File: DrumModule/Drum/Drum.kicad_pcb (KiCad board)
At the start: 2 copper layers, 39.4 x 99.1 mm, 44 parts, among them J1 Barrel_Jack_Switch, J2 Barrel_Jack_Switch, J3 Conn_02x05_Odd_Even, J4 Barrel_Jack_Switch, J5 Barrel_Jack_Switch, Q1 MMBT3904, Q2 MMBT3904, U1 74HC74, U2 MIC5205-5.0YM5, U3 LM2904DR, U4 LM2904DR

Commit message: Worked on the Drum
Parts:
- removed J4, J5: Barrel_Jack_Switch, Eurocad:PJ301M-12
- removed Q2: MMBT3904, Package_TO_SOT_SMD:SOT-23
- removed R13: 4.7M, Resistor_SMD:R_0805_2012Metric
- removed R14: 1k, Resistor_SMD:R_0805_2012Metric
- removed R15, R16, R17, R18: 10k, Resistor_SMD:R_0805_2012Metric
- added C14: 1uF, Capacitor_SMD:C_0805_2012Metric, F.Cu at (194.7, 91.9)
- added C15: 1uF, Capacitor_SMD:C_0805_2012Metric, F.Cu at (229.5, 65.7)
- added C16: 1uF, Capacitor_SMD:C_0805_2012Metric, F.Cu at (198.2, 91.9)
- added RV1: 5k, Eurocad:Alpha9mmPot, F.Cu at (210.4, 82.8)
- added RV2: 1M, Eurocad:Alpha9mmPot, F.Cu at (198.8, 69.7)
- added RV3: 50k, Eurocad:Alpha9mmPot, F.Cu at (222.0, 69.7)
- added RV4: 50k, Eurocad:Alpha9mmPot, F.Cu at (184.2, 101.6)
- added RV5: 50k, Eurocad:Alpha9mmPot, F.Cu at (210.4, 69.7)
- added U5: LM2904DR, Package_SO:SOIC-8_3.9x4.9mm_P1.27mm, F.Cu at (120.7, 73.7)
- C7: value 22nF -> 68nF
- C8: value 68nF -> 1uF
- C9: value 22nF -> 1uF
- R11, R3, R4: value 1M -> 10k
- R12: value 2k2 -> 10k
- R2: value 100k -> 1M
- R6: value 10k -> 1M
- R7: value 10k -> 1k
- R9: value 10k -> 5k
- moved J2 48.0 mm to (171.4, 55.9), turned to 180 degrees
- moved U3 39.7 mm to (118.1, 57.1)
- moved U1 31.2 mm to (127.0, 82.5)
- moved J1 0.57 mm to (144.8, 55.9), turned to 180 degrees
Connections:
- C10 pad 1: +12V -> Net-(C10-Pad1)
- C10 pad 2: GND -> Net-(C10-Pad2)
- C11 pad 1: GND -> +12V
- C11 pad 2: -12V -> GND
- C7 pad 2: Net-(C7-Pad2) -> Net-(C6-Pad1)
- C8 pad 1: Net-(C8-Pad1) -> +12V
- C8 pad 2: Net-(C6-Pad1) -> GND
- C9 pad 1: Net-(C9-Pad1) -> GND
- C9 pad 2: Net-(C7-Pad1) -> -12V
- J1 pad 1: Net-(J1-Pad1) -> GND
- J1 pad 2: GND -> Net-(J1-Pad2)
- J2 pad 1: Net-(J2-Pad1) -> GND
- J2 pad 2: GND -> Net-(J2-Pad2)
- J2 pad 3: Net-(J2-Pad3) -> Net-(C10-Pad2)
- Q1 pad 2: GND -> Net-(Q1-Pad2)
- Q1 pad 3: Net-(Q1-Pad3) -> +5V
- R1 pad 2: Net-(J1-Pad1) -> Net-(J1-Pad3)
- R10 pad 2: GND -> Net-(C10-Pad1)
- R11 pad 1: Net-(C6-Pad2) -> Net-(R11-Pad1)
- R11 pad 2: Net-(C8-Pad1) -> Net-(C15-Pad2)
- R12 pad 1: GND -> Net-(R12-Pad1)
- R12 pad 2: Net-(C6-Pad1) -> Net-(C16-Pad1)
- R2 pad 1: Net-(Q2-Pad1) -> Net-(Q1-Pad1)
- R2 pad 2: Net-(J2-Pad1) -> GND
- R3 pad 2: Net-(Q1-Pad1) -> Net-(Q1-Pad2)
- R4 pad 1: GND -> Net-(R4-Pad1)
- R4 pad 2: Net-(Q2-Pad1) -> Net-(R4-Pad2)
- R5 pad 1: Net-(Q1-Pad3) -> Net-(R4-Pad2)
- R5 pad 2: +5V -> GND
- R6 pad 1: Net-(Q2-Pad3) -> Net-(C6-Pad2)
- R6 pad 2: +5V -> Net-(R6-Pad2)
- R7 pad 2: Net-(R7-Pad2) -> Net-(C6-Pad1)
- R8 pad 1: Net-(R8-Pad1) -> Net-(C7-Pad1)
- R8 pad 2: Net-(R10-Pad1) -> Net-(R8-Pad2)
- R9 pad 1: Net-(R7-Pad2) -> Net-(R8-Pad2)
- R9 pad 2: GND -> Net-(R9-Pad2)
- U1 pad 10: +5V -> (no net)
- U1 pad 11: Net-(Q2-Pad3) -> (no net)
- U1 pad 12: Net-(U1-Pad12) -> (no net)
- U1 pad 13: +5V -> (no net)
- U1 pad 3: Net-(Q1-Pad3) -> Net-(Q1-Pad2)
- U1 pad 5: Net-(R7-Pad1) -> Net-(R4-Pad1)
- U1 pad 8: Net-(U1-Pad12) -> (no net)
- U1 pad 9: Net-(R8-Pad1) -> (no net)
- U3 pad 2: Net-(R15-Pad2) -> Net-(R8-Pad2)
- U3 pad 5: Net-(R7-Pad2) -> Net-(R4-Pad2)
- U3 pad 7: Net-(C8-Pad1) -> Net-(C7-Pad1)
- U4 pad 1: Net-(J5-Pad1) -> Net-(R10-Pad1)
- U4 pad 2: GND -> Net-(R10-Pad1)
- U4 pad 3: Net-(R16-Pad2) -> Net-(C15-Pad2)
- U4 pad 5: Net-(R10-Pad1) -> Net-(C16-Pad1)
- U4 pad 6: Net-(C7-Pad2) -> Net-(C15-Pad1)
- U4 pad 7: Net-(C9-Pad1) -> Net-(C15-Pad1)
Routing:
- net -12V: track 133.4 -> 53.0 mm
- net +12V: track 124.2 -> 76.9 mm, vias 7 -> 4
- net Net-(Q2-Pad3): track 39.4 -> 0.00 mm, vias 4 -> 0
- net +5V: track 81.7 -> 44.5 mm
- net Net-(RV3-Pad1): track 29.1 -> 0.00 mm, vias 2 -> 0
- net Net-(J5-Pad1): track 28.3 -> 0.00 mm, vias 2 -> 0
- net Net-(R10-Pad1): track 27.2 -> 54.1 mm, vias 2 -> 4
- net Net-(R7-Pad2): track 27.9 -> 2.12 mm, vias 2 -> 0
- net Net-(C8-Pad1): track 16.3 -> 0.00 mm
- net Net-(C15-Pad2): track 0.00 -> 10.5 mm
- net Net-(C6-Pad2): track 11.0 -> 21.3 mm, vias 0 -> 2
- net Net-(R15-Pad2): track 9.31 -> 0.00 mm, vias 1 -> 0
- net Net-(U1-Pad12): track 9.29 -> 0.00 mm
- net Net-(R16-Pad2): track 8.24 -> 0.00 mm
- net Net-(Q1-Pad3): track 18.1 -> 11.7 mm
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
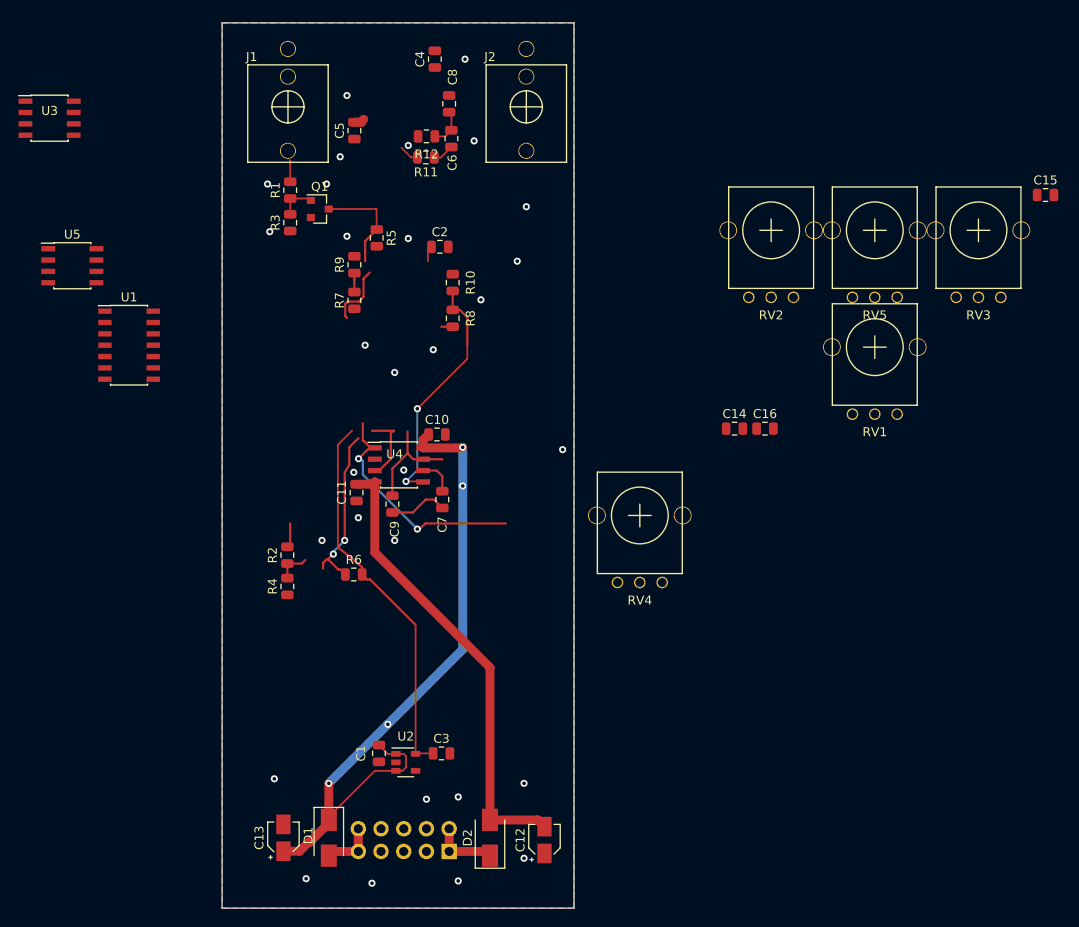
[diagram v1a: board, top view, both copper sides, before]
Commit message: Organized layout of drum, should be ready for routing.
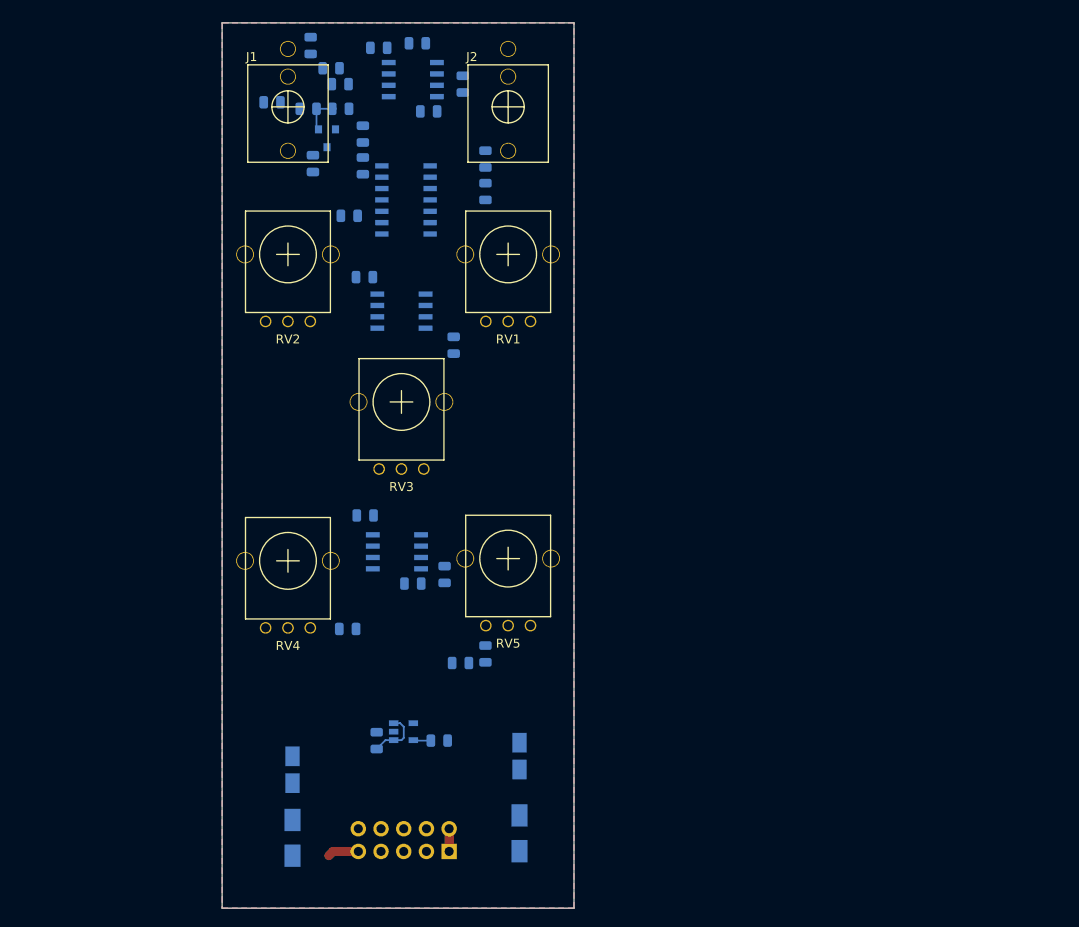
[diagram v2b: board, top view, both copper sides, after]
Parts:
- C1, C10, C11, C12, C13, C14, C15, C16, C2, C3, C4, C5, C6, C7, C8, C9, D1, D2, Q1, R1, R10, R11, R12, R2, R3, R4, R5, R6, R7, R8, R9, U1, U2, U3, U4, U5: moved to B.Cu
- moved C15 79.5 mm to (162.3, 108.2), turned to 270 degrees
- moved RV3 67.4 mm to (157.5, 88.9)
- moved R12 58.3 mm to (166.9, 117.1), turned to 270 degrees
- moved R6 56.7 mm to (149.6, 51.6), turned to 180 degrees
- moved RV5 55.1 mm to (169.4, 106.4)
- moved RV2 54.1 mm to (144.8, 72.4)
- moved C8 53.8 mm to (158.8, 109.2), turned to 180 degrees
- moved R11 53.5 mm to (151.5, 114.3), turned to 0 degrees
- moved C7 52.9 mm to (147.3, 49.0), turned to 270 degrees
- moved R4 47.8 mm to (153.2, 62.5)
- moved C14 44.7 mm to (153.3, 74.9)
- moved R2 43.9 mm to (147.6, 62.2), turned to 270 degrees
- moved C16 43.0 mm to (164.1, 118.1), turned to 180 degrees
- moved RV1 42.3 mm to (169.4, 72.4)
- moved U3 40.9 mm to (158.8, 52.8), turned to 180 degrees
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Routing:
- net +12V: track 76.9 -> 6.09 mm, vias 4 -> 0
- net Net-(R10-Pad1): track 54.1 -> 0.00 mm, vias 4 -> 0
- net -12V: track 53.0 -> 0.00 mm
- net +5V: track 44.5 -> 1.98 mm
- net Net-(C6-Pad2): track 21.3 -> 0.00 mm, vias 2 -> 0
- net Net-(C9-Pad1): track 12.1 -> 0.00 mm
- net Net-(Q1-Pad3): track 11.7 -> 0.00 mm
- net Net-(C15-Pad2): track 10.5 -> 0.00 mm
- net Net-(C7-Pad1): track 7.85 -> 0.00 mm
- net Net-(U1-Pad2): track 7.04 -> 0.00 mm
- net Net-(D2-Pad1): track 7.31 -> 2.54 mm
- net Net-(C6-Pad1): track 4.26 -> 0.00 mm
- net Net-(C7-Pad2): track 4.09 -> 0.00 mm
- net Net-(Q2-Pad1): track 3.79 -> 0.00 mm
- net GND: track 2.75 -> 0.00 mm, vias 30 -> 0
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
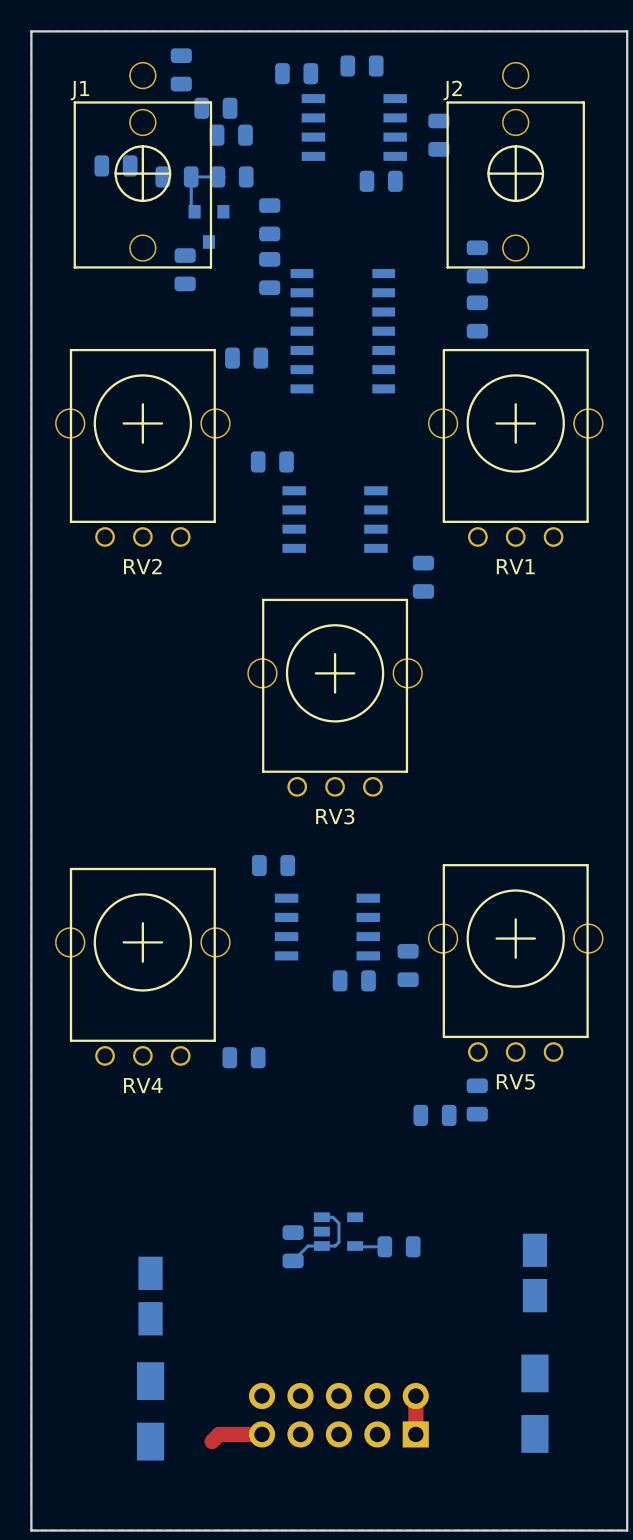
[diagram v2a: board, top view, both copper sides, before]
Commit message: worked on the layout of the drum
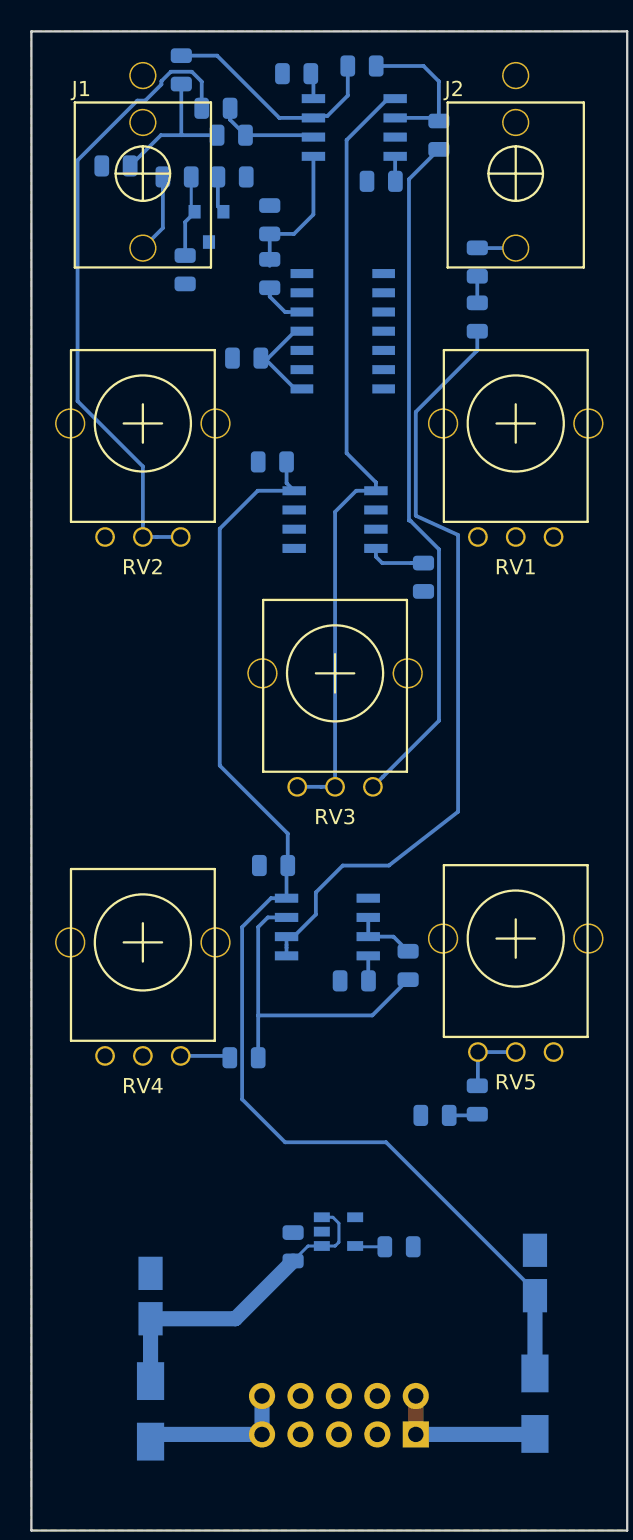
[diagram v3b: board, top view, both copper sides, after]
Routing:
- net -12V: track 0.00 -> 81.2 mm
- net Net-(RV3-Pad1): track 0.00 -> 52.3 mm
- net Net-(R10-Pad1): track 0.00 -> 51.9 mm
- net Net-(R9-Pad2): track 0.00 -> 45.6 mm
- net Net-(R6-Pad2): track 0.00 -> 42.0 mm
- net +12V: track 6.09 -> 28.4 mm
- net Net-(C15-Pad2): track 0.00 -> 21.7 mm
- net Net-(C7-Pad1): track 0.00 -> 15.3 mm
- net Net-(R8-Pad2): track 0.00 -> 10.2 mm
- net Net-(C6-Pad1): track 0.00 -> 9.97 mm
- net Net-(R4-Pad2): track 0.00 -> 9.37 mm
- net Net-(D2-Pad1): track 2.54 -> 10.4 mm
- net +5V: track 1.98 -> 8.99 mm
- net Net-(C6-Pad2): track 0.00 -> 6.85 mm
- net Net-(D1-Pad2): track 3.50 -> 10.1 mm
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
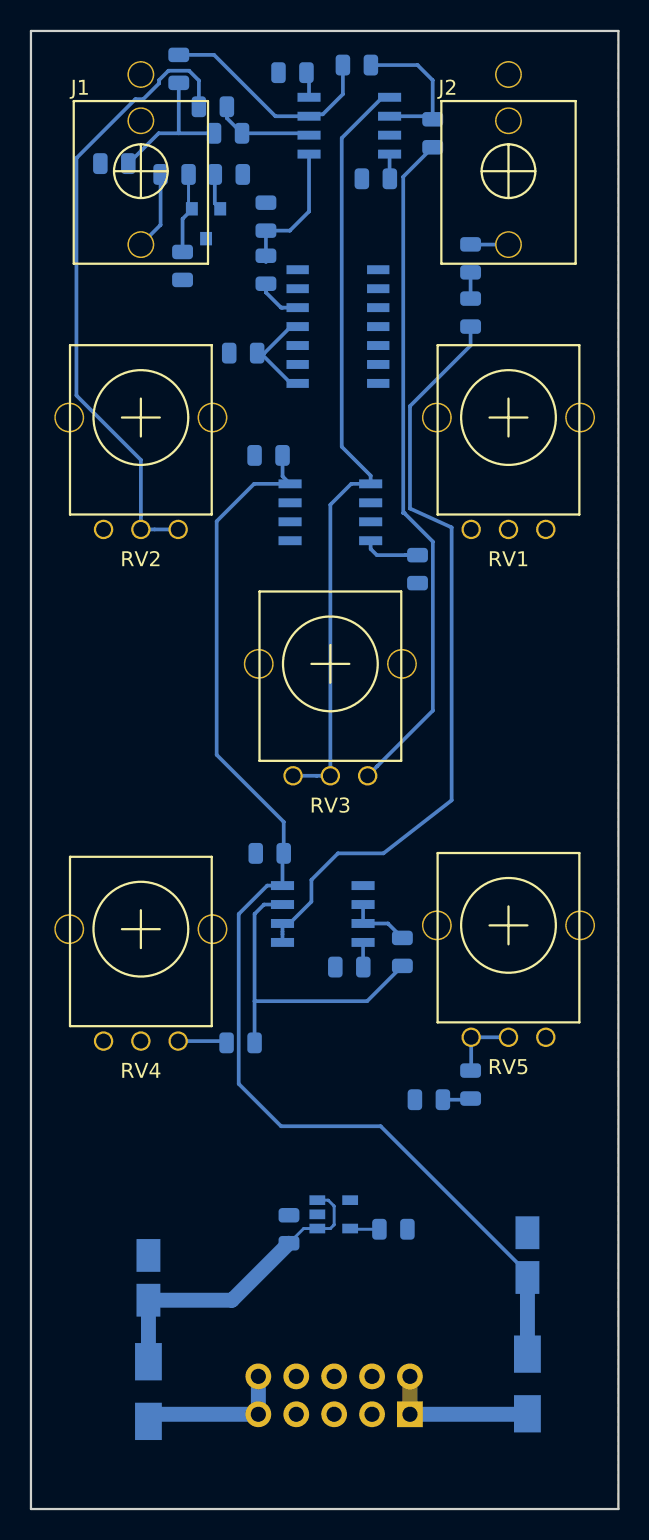
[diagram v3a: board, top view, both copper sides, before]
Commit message: Finished off the drum
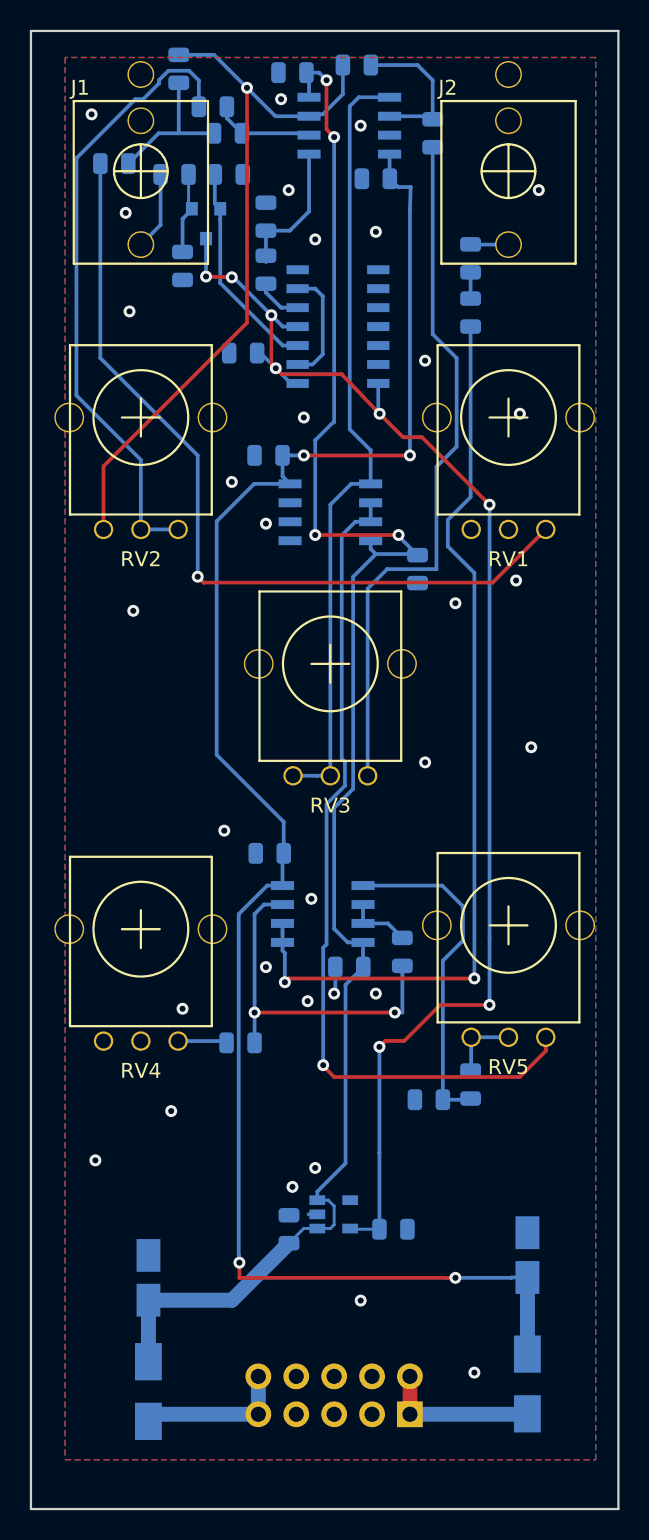
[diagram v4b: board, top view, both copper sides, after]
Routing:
- net +12V: track 28.4 -> 114.5 mm, vias 0 -> 4
- net +5V: track 8.99 -> 94.4 mm, vias 0 -> 8
- net Net-(RV5-Pad3): track 0.00 -> 56.7 mm, vias 0 -> 1
- net Net-(R7-Pad1): track 0.00 -> 55.4 mm, vias 0 -> 1
- net -12V: track 81.2 -> 117.1 mm, vias 0 -> 4
- net Net-(C7-Pad1): track 15.3 -> 48.8 mm, vias 0 -> 1
- net Net-(C16-Pad1): track 1.89 -> 22.7 mm
- net Net-(Q1-Pad2): track 2.45 -> 14.4 mm
- net Net-(R10-Pad1): track 51.9 -> 61.9 mm, vias 0 -> 2
- net Net-(U1-Pad2): track 0.00 -> 7.75 mm
- net GND: track 0.00 -> 2.40 mm, vias 0 -> 32
- net Net-(C15-Pad2): track 21.7 -> 23.8 mm, vias 0 -> 2
- net Net-(R9-Pad2): track 45.6 -> 47.2 mm
